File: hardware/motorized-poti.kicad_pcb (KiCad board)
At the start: 2 copper layers, 100 x 20 mm, 31 parts, among them J1 AKL_5_2, P1 CON-SENSOR2, P2 MOTORIZED_POTI, P3 BOOT, P4 CONN_02X04, P5 CONN_02X04, U1 XMC1XXX24, U2 ZXBM5210, U3 DRILL, U4 DRILL, U5 DRILL, U6 DRILL

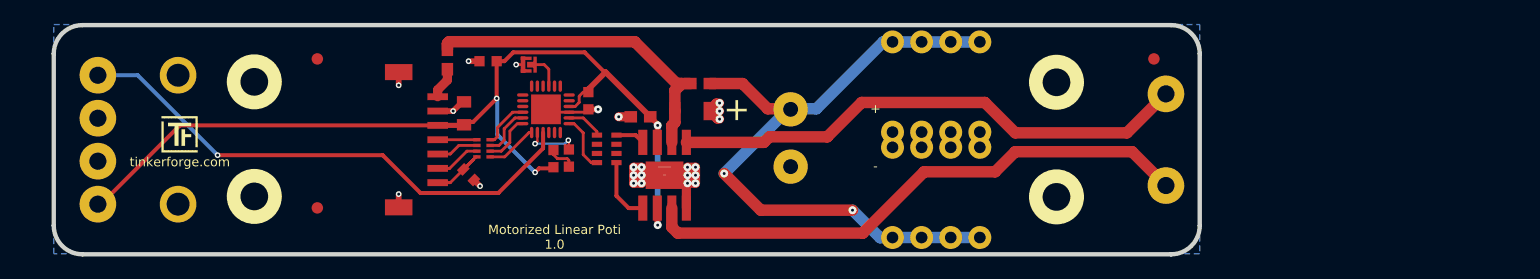
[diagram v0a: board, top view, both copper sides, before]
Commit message: modified prototype:
* increase PCB length
* change position of bricklet connector
* add buffer for analog signal
* remove external power input
* fixed 5V supply over bricklet connector
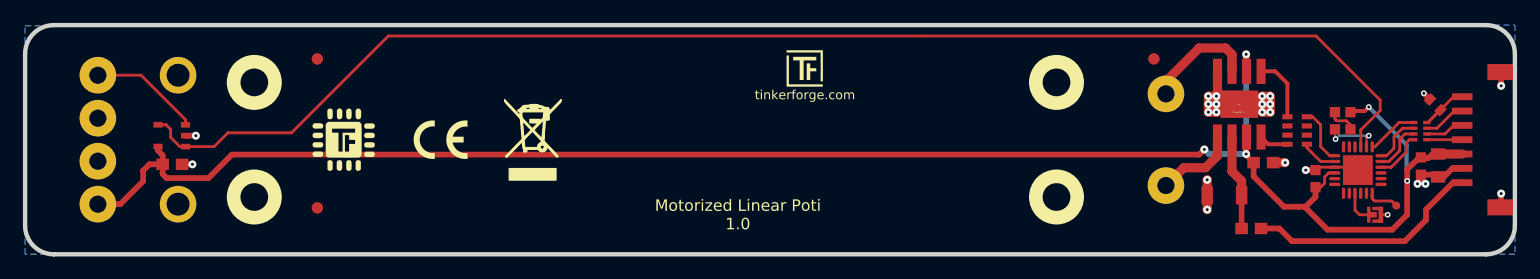
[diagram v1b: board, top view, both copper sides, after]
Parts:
- removed J1: AKL_5_2, AKL_5_2
- removed L2: FB, C0603E
- removed P4, P5: CONN_02X04, kicad-libraries:pin_array_4x2_388
- added C101: 100nF, kicad-libraries:C0603E, F.Cu at (88.0, 102.8)
- added J101: Debug, DEBUG_PAD, F.Cu at (194.8, 106.4)
- added U101: TLV271, kicad-libraries:SOT23-5, F.Cu at (87.9, 100.3)
- G*** (x2), VAL: moved to F.Cu
- U2: footprint kicad-libraries:SO-8-EP -> SO-8-EP
- moved P1 98.6 mm to (205.1, 100.7), turned to 90 degrees
- moved C2 85.1 mm to (198.4, 102.9), turned to 270 degrees
- moved C6 84.6 mm to (198.2, 97.6), turned to 135 degrees
- moved C5 81.9 mm to (196.9, 103.0), turned to 270 degrees
- moved RP3 81.8 mm to (196.8, 99.9), turned to 90 degrees
- moved P3 75.0 mm to (192.9, 107.2), turned to 180 degrees
- moved L1 71.7 mm to (182.1, 108.4), turned to 180 degrees
- moved U1 71.0 mm to (191.4, 103.3), turned to 270 degrees
- moved D1 69.6 mm to (190.8, 99.0), turned to 270 degrees
- moved R1 66.9 mm to (189.4, 99.0), turned to 270 degrees
- moved C4 63.8 mm to (187.7, 104.0), turned to 90 degrees
- moved RP1 60.3 mm to (186.1, 99.8), turned to 90 degrees
- moved G*** 54.9 mm to (141.6, 92.8)
- moved C1 54.5 mm to (183.2, 102.7), turned to 0 degrees
- moved U2 50.5 mm to (181.1, 97.5), turned to 0 degrees
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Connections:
- P2 pad 2: Net-(P2-Pad2) -> (no net)
- P2 pad 4: AIN -> Net-(P2-Pad4)
- RP1 pad 2: Net-(RP1-Pad2) -> (no net)
- RP1 pad 3: Net-(RP1-Pad3) -> (no net)
- RP1 pad 6: Net-(RP1-Pad6) -> (no net)
- RP1 pad 7: Net-(RP1-Pad7) -> (no net)
- U1 pad 11: Net-(U1-Pad11) -> (no net)
- U1 pad 12: Net-(U1-Pad12) -> (no net)
- U1 pad 13: Net-(U1-Pad13) -> (no net)
- U1 pad 14: Net-(U1-Pad14) -> (no net)
- U1 pad 16: Net-(U1-Pad16) -> (no net)
- U1 pad 17: Net-(U1-Pad17) -> (no net)
- U1 pad 19: Net-(U1-Pad19) -> (no net)
- U1 pad 20: Net-(U1-Pad20) -> (no net)
- U1 pad 21: Net-(U1-Pad21) -> (no net)
- U1 pad 4: Net-(U1-Pad4) -> (no net)
- U1 pad 5: Net-(U1-Pad5) -> (no net)
- U1 pad 6: Net-(U1-Pad6) -> (no net)
- U2 pad 1: Net-(P2-PadA) -> Net-(P2-PadB)
- U2 pad 7: Net-(P2-PadB) -> Net-(P2-PadA)
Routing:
- net VCC: track 85.1 -> 160.4 mm, vias 4 -> 5
- net AIN: track 46.1 -> 118.9 mm, vias 1 -> 0
- net PWR: track 59.7 -> 0.00 mm, vias 2 -> 0
- net Net-(P2-PadB): track 49.9 -> 7.21 mm
- net Net-(P2-PadA): track 46.8 -> 9.77 mm
- net Net-(C3-Pad2): track 29.4 -> 9.58 mm
- net +5V: track 2.75 -> 20.6 mm
- net Net-(P2-Pad4): track 0.00 -> 9.70 mm
- net GND: track 38.1 -> 42.1 mm, vias 23 -> 24
- net Net-(J101-Pad1): track 0.00 -> 2.82 mm
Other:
- board size 100 x 20 mm -> 130 x 20 mm
- board text added: "Copyright Tinkerforge GmbH 2017. This documentation describes Open Hardware and is licensed under the CERN OHL v. 1.1. You may redistribute and modify this documentation under the terms of the CERN OHL v.1.1. (http://ohwr.org/cernohl). This documentation is distributed WITHOUT ANY EXPRESS OR IMPLIED WARRANTY, INCLUDING OF MERCHANTABILITY, SATISFACTORY QUALITY AND FITNESS FOR A PARTICULAR PURPOSE.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"
- board text removed: "+"
- board text removed: "-"
- board text removed: "Copyright Tinkerforge GmbH 2015. This documentation describes Open Hardware and is licensed under the CERN OHL v. 1.1. You may redistribute and modify this documentation under the terms of the CERN OHL v.1.1. (http://ohwr.org/cernohl). This documentation is distributed WITHOUT ANY EXPRESS OR IMPLIED WARRANTY, INCLUDING OF MERCHANTABILITY, SATISFACTORY QUALITY AND FITNESS FOR A PARTICULAR PURPOSE.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"

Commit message: specify filter circuit
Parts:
- C6: value TBD -> 220pF
- RP3: value TBD -> 82
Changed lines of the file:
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@@
-(kicad_pcb (version 4) (host pcbnew 4.0.6-e0-6349~53~ubuntu16.04.1)
+(kicad_pcb (version 4) (host pcbnew 4.0.7-e0-6372~58~ubuntu16.10.1)
   (general
     (links 58)
@@
   )
   (setup
-    (last_trace_width 0.25)
+    (last_trace_width 0.249)
     (user_trace_width 0.2)
     (user_trace_width 0.25)
@@
       (effects (font (size 0.2 0.2) (thickness 0.05)))
     )
-    (fp_text value TBD (at 0 -0.275 135) (layer F.Fab)
+    (fp_text value 220pF (at 0 -0.275 135) (layer F.Fab)
       (effects (font (size 0.2 0.2) (thickness 0.05)))
     )
@@
       (effects (font (size 0.2 0.2) (thickness 0.05)))
     )
-    (fp_text value TBD (at -0.025 -0.45 90) (layer F.Fab)
+    (fp_text value 82 (at -0.025 -0.45 90) (layer F.Fab)
       (effects (font (size 0.2 0.2) (thickness 0.05)))
     )

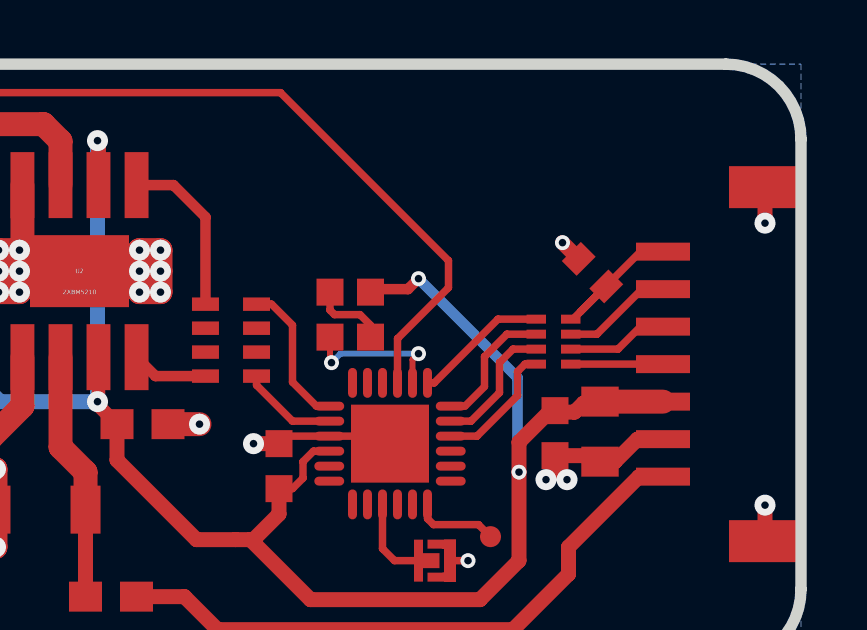
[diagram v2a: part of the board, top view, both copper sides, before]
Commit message: add status led description text
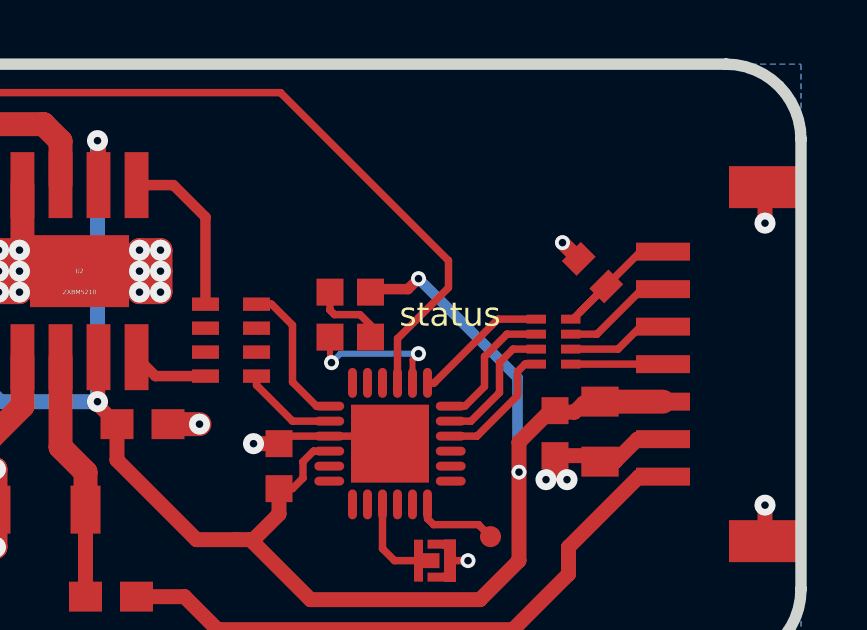
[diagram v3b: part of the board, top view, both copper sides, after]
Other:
- board text added: "status"
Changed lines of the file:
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@@
-(kicad_pcb (version 4) (host pcbnew 4.0.7-e0-6372~58~ubuntu16.10.1)
+(kicad_pcb (version 4) (host pcbnew 4.0.7-e2-6376~58~ubuntu17.04.1)
   (general
     (links 58)
     (no_connects 0)
-    (area 74.909499 90.459499 205.290501 110.840501)
+    (area 70.875139 90.459499 282.795857 162.890793)
     (thickness 1.6002)
-    (drawings 11)
+    (drawings 12)
     (tracks 248)
     (zones 0)
@@
     )
   )
+  (gr_text status (at 193.4 99) (layer F.SilkS)
+    (effects (font (size 0.8 0.8) (thickness 0.14986)))
+  )
   (gr_line (start 202.6 110.65) (end 77.6 110.65) (angle 90) (layer Edge.Cuts) (width 0.381))

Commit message: specify processor
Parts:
- U1: value XMC1XXX24 -> XMC1100-16
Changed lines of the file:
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@@
       (effects (font (size 0.3 0.3) (thickness 0.075)))
     )
-    (fp_text value XMC1XXX24 (at 0 0.8 270) (layer F.Fab)
+    (fp_text value XMC1100-16 (at 0 0.8 270) (layer F.Fab)
       (effects (font (size 0.3 0.3) (thickness 0.075)))
     )

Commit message: Add 3d information (final)
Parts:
- P2: footprint MOTORIZED_POTI -> kicad-libraries:MOTORIZED_POTI
- RP3: footprint 4X0402 -> kicad-libraries:4X0402
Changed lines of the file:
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@@
-(kicad_pcb (version 4) (host pcbnew 4.0.7-e2-6376~58~ubuntu17.04.1)
+(kicad_pcb (version 4) (host pcbnew 4.0.2+dfsg1-stable)
   (general
     (links 58)
     (no_connects 0)
-    (area 70.875139 90.459499 282.795857 162.890793)
+    (area 74.909499 90.459499 205.290501 110.840501)
     (thickness 1.6002)
     (drawings 12)
@@
     (add_net VCC)
   )
-  (module MOTORIZED_POTI (layer Rückseite)
-    (at 145.1 100.65)
-    (fp_text reference P2 (at 0 -1.34) (layer B.Fab)
-      (effects (font (size 1 1) (thickness 0.15)) (justify mirror))
-    )
-    (fp_text value MOTORIZED_POTI (at 0 0.5) (layer B.Fab)
-      (effects (font (size 1 1) (thickness 0.15)) (justify mirror))
-    )
-    (fp_line (start 72.5 -9) (end 72.5 9) (layer B.Fab) (width 0.15))
-    (fp_line (start 72.5 9) (end -74 9) (layer B.Fab) (width 0.15))
-    (fp_line (start -74 9) (end -74 -9) (layer B.Fab) (width 0.15))
-    (fp_line (start -74 -9) (end 72.5 -9) (layer B.Fab) (width 0.15))
-    (pad 1 thru_hole circle (at -63.65 5.625) (size 3.2 3.2) (drill 1.5) (layers *.Cu *.Mask B.SilkS)
-      (net 8 VCC))
-    (pad 2 thru_hole circle (at -63.65 1.875) (size 3.2 3.2) (drill 1.5) (layers *.Cu *.Mask B.SilkS))
-    (pad 3 thru_hole circle (at -63.65 -1.875) (size 3.2 3.2) (drill 1.5) (layers *.Cu *.Mask B.SilkS)
-      (net 1 GND))
-    (pad 4 thru_hole circle (at -63.65 -5.625) (size 3.2 3.2) (drill 1.5) (layers *.Cu *.Mask B.SilkS)
-      (net 24 "Net-(P2-Pad4)"))
-    (pad "" thru_hole circle (at -56.65 5.625) (size 3.2 3.2) (drill 2) (layers *.Cu *.Mask B.SilkS))
-    (pad "" thru_hole circle (at -56.65 -5.625) (size 3.2 3.2) (drill 2) (layers *.Cu *.Mask B.SilkS))
-    (pad A thru_hole circle (at 29.55 -4) (size 3.2 3.2) (drill 1.5) (layers *.Cu *.Mask B.SilkS)
-      (net 4 "Net-(P2-PadA)"))
-    (pad B thru_hole circle (at 29.55 4) (size 3.2 3.2) (drill 1.5) (layers *.Cu *.Mask B.SilkS)
-      (net 5 "Net-(P2-PadB)"))
-  )
   (module kicad-libraries:C1206 (layer Vorderseite)
     (at 179.75 105.5)
@@
     )
   )
-  (module 4X0402 (layer Vorderseite)
-    (at 196.85 99.9 90)
-    (attr smd)
-    (fp_text reference RP3 (at -0.025 0.25 90) (layer F.Fab)
-      (effects (font (size 0.2 0.2) (thickness 0.05)))
-    )
-    (fp_text value 82 (at -0.025 -0.45 90) (layer F.Fab)
-      (effects (font (size 0.2 0.2) (thickness 0.05)))
-    )
-    (fp_line (start -1.04902 -0.89916) (end 1.04902 -0.89916) (layer F.Fab) (width 0.001))
-    (fp_line (start 1.04902 -0.89916) (end 1.04902 0.89916) (layer F.Fab) (width 0.001))
-    (fp_line (start -1.04902 0.89916) (end 1.04902 0.89916) (layer F.Fab) (width 0.001))
-    (fp_line (start -1.04902 -0.89916) (end -1.04902 0.89916) (layer F.Fab) (width 0.001))
-    (pad 1 smd rect (at -0.7493 0.575 270) (size 0.29972 0.65) (layers Vorderseite F.Paste F.Mask)
-      (net 20 "Net-(P1-Pad4)"))
-    (pad 2 smd rect (at -0.24892 0.575 270) (size 0.29972 0.65) (layers Vorderseite F.Paste F.Mask)
-      (net 21 "Net-(P1-Pad5)"))
-    (pad 3 smd rect (at 0.24892 0.575 270) (size 0.29972 0.65) (layers Vorderseite F.Paste F.Mask)
-      (net 22 "Net-(P1-Pad6)"))
-    (pad 4 smd rect (at 0.7493 0.575 270) (size 0.29972 0.65) (layers Vorderseite F.Paste F.Mask)
-      (net 19 "Net-(C6-Pad1)"))
-    (pad 5 smd rect (at 0.7493 -0.575 90) (size 0.29972 0.65) (layers Vorderseite F.Paste F.Mask)
-      (net 10 S-MISO))
-    (pad 6 smd rect (at 0.24892 -0.575 90) (size 0.29972 0.65) (layers Vorderseite F.Paste F.Mask)
-      (net 11 S-MOSI))
-    (pad 7 smd rect (at -0.24892 -0.575 90) (size 0.29972 0.65) (layers Vorderseite F.Paste F.Mask)
-      (net 12 S-CLK))
-    (pad 8 smd rect (at -0.7493 -0.575 90) (size 0.29972 0.65) (layers Vorderseite F.Paste F.Mask)
-      (net 13 S-CS))
-  )
   (module SO-8-EP (layer Vorderseite)
     (at 181.05 97.55)
@@
     )
   )
+  (module kicad-libraries:4X0402 (layer Vorderseite)
+    (at 196.85 99.9 90)
+    (attr smd)
+    (fp_text reference RP3 (at -0.025 0.25 90) (layer F.Fab)
+      (effects (font (size 0.2 0.2) (thickness 0.05)))
+    )
+    (fp_text value 82 (at -0.025 -0.45 90) (layer F.Fab)
+      (effects (font (size 0.2 0.2) (thickness 0.05)))
+    )
+    (fp_line (start -1.04902 -0.89916) (end 1.04902 -0.89916) (layer F.Fab) (width 0.001))
+    (fp_line (start 1.04902 -0.89916) (end 1.04902 0.89916) (layer F.Fab) (width 0.001))
+    (fp_line (start -1.04902 0.89916) (end 1.04902 0.89916) (layer F.Fab) (width 0.001))
+    (fp_line (start -1.04902 -0.89916) (end -1.04902 0.89916) (layer F.Fab) (width 0.001))
+    (pad 1 smd rect (at -0.7493 0.575 270) (size 0.29972 0.65) (layers Vorderseite F.Paste F.Mask)
+      (net 20 "Net-(P1-Pad4)"))
+    (pad 2 smd rect (at -0.24892 0.575 270) (size 0.29972 0.65) (layers Vorderseite F.Paste F.Mask)
+      (net 21 "Net-(P1-Pad5)"))
+    (pad 3 smd rect (at 0.24892 0.575 270) (size 0.29972 0.65) (layers Vorderseite F.Paste F.Mask)
+      (net 22 "Net-(P1-Pad6)"))
+    (pad 4 smd rect (at 0.7493 0.575 270) (size 0.29972 0.65) (layers Vorderseite F.Paste F.Mask)
+      (net 19 "Net-(C6-Pad1)"))
+    (pad 5 smd rect (at 0.7493 -0.575 90) (size 0.29972 0.65) (layers Vorderseite F.Paste F.Mask)
+      (net 10 S-MISO))
+    (pad 6 smd rect (at 0.24892 -0.575 90) (size 0.29972 0.65) (layers Vorderseite F.Paste F.Mask)
+      (net 11 S-MOSI))
+    (pad 7 smd rect (at -0.24892 -0.575 90) (size 0.29972 0.65) (layers Vorderseite F.Paste F.Mask)
+      (net 12 S-CLK))
+    (pad 8 smd rect (at -0.7493 -0.575 90) (size 0.29972 0.65) (layers Vorderseite F.Paste F.Mask)
+      (net 13 S-CS))
+    (model Resistors_SMD/R_4x0402.wrl
+      (at (xyz 0 0 0))
+      (scale (xyz 1 1 1))
+      (rotate (xyz 0 0 90))
+    )
+  )
+  (module kicad-libraries:MOTORIZED_POTI (layer Rückseite)
+    (at 145.1 100.65)
+    (fp_text reference P2 (at 0 -1.34) (layer B.Fab)
+      (effects (font (size 1 1) (thickness 0.15)) (justify mirror))
+    )
+    (fp_text value MOTORIZED_POTI (at 0 0.5) (layer B.Fab)
+      (effects (font (size 1 1) (thickness 0.15)) (justify mirror))
+    )
+    (fp_line (start 72.5 -9) (end 72.5 9) (layer B.Fab) (width 0.15))
+    (fp_line (start 72.5 9) (end -74 9) (layer B.Fab) (width 0.15))
+    (fp_line (start -74 9) (end -74 -9) (layer B.Fab) (width 0.15))
+    (fp_line (start -74 -9) (end 72.5 -9) (layer B.Fab) (width 0.15))
+    (pad 1 thru_hole circle (at -63.65 5.625) (size 3.2 3.2) (drill 1.5) (layers *.Cu *.Mask B.SilkS)
+      (net 8 VCC))
+    (pad 2 thru_hole circle (at -63.65 1.875) (size 3.2 3.2) (drill 1.5) (layers *.Cu *.Mask B.SilkS))
+    (pad 3 thru_hole circle (at -63.65 -1.875) (size 3.2 3.2) (drill 1.5) (layers *.Cu *.Mask B.SilkS)
+      (net 1 GND))
+    (pad 4 thru_hole circle (at -63.65 -5.625) (size 3.2 3.2) (drill 1.5) (layers *.Cu *.Mask B.SilkS)
+      (net 24 "Net-(P2-Pad4)"))
+    (pad "" thru_hole circle (at -56.65 5.625) (size 3.2 3.2) (drill 2) (layers *.Cu *.Mask B.SilkS))
+    (pad "" thru_hole circle (at -56.65 -5.625) (size 3.2 3.2) (drill 2) (layers *.Cu *.Mask B.SilkS))
+    (pad A thru_hole circle (at 29.55 -4) (size 3.2 3.2) (drill 1.5) (layers *.Cu *.Mask B.SilkS)
+      (net 4 "Net-(P2-PadA)"))
+    (pad B thru_hole circle (at 29.55 4) (size 3.2 3.2) (drill 1.5) (layers *.Cu *.Mask B.SilkS)
+      (net 5 "Net-(P2-PadB)"))
+    (model Potentiometers/RSA0N11M9A0J.wrl
+      (at (xyz 0 0 1))
+      (scale (xyz 1 1 1))
+      (rotate (xyz 90 180 0))
+    )
+  )

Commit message: change dnp l1 to fb
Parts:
- L1: value DNP -> FB
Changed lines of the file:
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@@
-(kicad_pcb (version 4) (host pcbnew 4.0.2+dfsg1-stable)
+(kicad_pcb (version 4) (host pcbnew 4.0.7-e2-6376~58~ubuntu17.04.1)
   (general
     (links 58)
     (no_connects 0)
-    (area 74.909499 90.459499 205.290501 110.840501)
+    (area 70.875139 90.459499 282.795857 162.890793)
     (thickness 1.6002)
     (drawings 12)
@@
   )
   (setup
-    (last_trace_width 0.249)
+    (last_trace_width 0.5)
     (user_trace_width 0.2)
     (user_trace_width 0.25)
@@
     (add_net VCC)
   )
+  (module C0603E (layer Vorderseite)
+    (at 182.1 108.4 180)
+    (attr smd)
+    (fp_text reference L1 (at 0.05 0.225 180) (layer F.Fab)
+      (effects (font (size 0.2 0.2) (thickness 0.05)))
+    )
+    (fp_text value FB (at 0.05 -0.375 180) (layer F.Fab)
+      (effects (font (size 0.2 0.2) (thickness 0.05)))
+    )
+    (fp_line (start -1.45034 -0.65024) (end 1.45034 -0.65024) (layer F.Fab) (width 0.001))
+    (fp_line (start 1.45034 -0.65024) (end 1.45034 0.65024) (layer F.Fab) (width 0.001))
+    (fp_line (start 1.45034 0.65024) (end -1.45034 0.65024) (layer F.Fab) (width 0.001))
+    (fp_line (start -1.45034 0.65024) (end -1.45034 -0.65024) (layer F.Fab) (width 0.001))
+    (pad 1 smd rect (at -0.8501 0 180) (size 1.1 1) (layers Vorderseite F.Paste F.Mask)
+      (net 2 +5V))
+    (pad 2 smd rect (at 0.8501 0 180) (size 1.1 1) (layers Vorderseite F.Paste F.Mask)
+      (net 9 "Net-(C3-Pad2)"))
+    (model Capacitors_SMD/C_0603.wrl
+      (at (xyz 0 0 0))
+      (scale (xyz 1 1 1))
+      (rotate (xyz 0 0 0))
+    )
+  )
   (module kicad-libraries:C1206 (layer Vorderseite)
     (at 179.75 105.5)
@@
     )
   )
-  (module C0603E (layer Vorderseite)
-    (at 182.1 108.4 180)
-    (attr smd)
-    (fp_text reference L1 (at 0.05 0.225 180) (layer F.Fab)
-      (effects (font (size 0.2 0.2) (thickness 0.05)))
-    )
-    (fp_text value DNP (at 0.05 -0.375 180) (layer F.Fab)
-      (effects (font (size 0.2 0.2) (thickness 0.05)))
-    )
-    (fp_line (start -1.45034 -0.65024) (end 1.45034 -0.65024) (layer F.Fab) (width 0.001))
-    (fp_line (start 1.45034 -0.65024) (end 1.45034 0.65024) (layer F.Fab) (width 0.001))
-    (fp_line (start 1.45034 0.65024) (end -1.45034 0.65024) (layer F.Fab) (width 0.001))
-    (fp_line (start -1.45034 0.65024) (end -1.45034 -0.65024) (layer F.Fab) (width 0.001))
-    (pad 1 smd rect (at -0.8501 0 180) (size 1.1 1) (layers Vorderseite F.Paste F.Mask)
-      (net 2 +5V))
-    (pad 2 smd rect (at 0.8501 0 180) (size 1.1 1) (layers Vorderseite F.Paste F.Mask)
-      (net 9 "Net-(C3-Pad2)"))
-    (model Capacitors_SMD/C_0603.wrl
-      (at (xyz 0 0 0))
-      (scale (xyz 1 1 1))
-      (rotate (xyz 0 0 0))
-    )
-  )
   (module CON-SENSOR2 (layer Vorderseite)
     (at 205.1 100.65 90)
@@
   (segment (start 183.75 98.25) (end 183.75 97.55) (width 0.8001) (layer Vorderseite) (net 1))
   (segment (start 192.05 103.95) (end 192.05 102.65) (width 0.35052) (layer Vorderseite) (net 1))
-  (segment (start 200.5 104.4) (end 199.7 104.4) (width 0.5) (layer Vorderseite) (net 2))
   (segment (start 199.7 104.4) (end 197.35 106.75) (width 0.5) (layer Vorderseite) (net 2))
-  (segment (start 197.35 106.75) (end 197.35 107.65) (width 0.5) (layer Vorderseite) (net 2))
-  (segment (start 197.35 107.65) (end 195.5 109.5) (width 0.5) (layer Vorderseite) (net 2))
-  (segment (start 195.5 109.5) (end 185.65 109.5) (width 0.5) (layer Vorderseite) (net 2))
-  (segment (start 185.65 109.5) (end 184.55 108.4) (width 0.5) (layer Vorderseite) (net 2))
   (segment (start 184.55 108.4) (end 182.9501 108.4) (width 0.5) (layer Vorderseite) (net 2))
+  (segment (start 185.65 109.5) (end 184.55 108.4) (width 0.5) (layer Vorderseite) (net 2))
+  (segment (start 195.5 109.5) (end 185.65 109.5) (width 0.5) (layer Vorderseite) (net 2))
+  (segment (start 197.35 107.65) (end 195.5 109.5) (width 0.5) (layer Vorderseite) (net 2))
+  (segment (start 197.35 106.75) (end 197.35 107.65) (width 0.5) (layer Vorderseite) (net 2))
+  (segment (start 200.5 104.4) (end 199.7 104.4) (width 0.5) (layer Vorderseite) (net 2))
   (segment (start 89.09888 101.24996) (end 91.60004 101.24996) (width 0.25) (layer Vorderseite) (net 3))
   (segment (start 106.8 91.6) (end 153.25 91.6) (width 0.25) (layer Vorderseite) (net 3))
@@
   (segment (start 181.68246 102.03256) (end 182.2999 102.65) (width 0.45) (layer Vorderseite) (net 8))
   (segment (start 198.7499 101.9) (end 198.55 102.0999) (width 0.45) (layer Vorderseite) (net 8))
+  (segment (start 181.2499 108.4) (end 181.2499 105.50124) (width 0.5) (layer Vorderseite) (net 9))
   (segment (start 180.41754 100.41766) (end 180.41754 103.4164) (width 0.8001) (layer Vorderseite) (net 9))
   (segment (start 180.41754 103.4164) (end 181.25114 104.25) (width 0.8001) (layer Vorderseite) (net 9))
   (segment (start 181.25114 104.25) (end 181.25114 105.5) (width 0.8001) (layer Vorderseite) (net 9))
   (segment (start 181.25114 105.5) (end 181.25114 104.25) (width 0.5) (layer Vorderseite) (net 9))
-  (segment (start 181.2499 108.4) (end 181.2499 105.50124) (width 0.5) (layer Vorderseite) (net 9))
   (segment (start 181.2499 105.50124) (end 181.25114 105.5) (width 0.5) (layer Vorderseite) (net 9))
   (segment (start 196.275 99.1507) (end 194.9993 99.1507) (width 0.25) (layer Vorderseite) (net 10))

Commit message: specify opamp more precise
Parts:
- U101: value TLV271 -> TLV271IDBVR
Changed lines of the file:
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@@
   )
   (setup
-    (last_trace_width 0.5)
+    (last_trace_width 0.249)
     (user_trace_width 0.2)
     (user_trace_width 0.25)
@@
       (effects (font (size 0.2 0.2) (thickness 0.05)))
     )
-    (fp_text value TLV271 (at -0.03 -0.38 90) (layer F.Fab)
+    (fp_text value TLV271IDBVR (at -0.03 -0.38 90) (layer F.Fab)
       (effects (font (size 0.2 0.2) (thickness 0.05)))
     )
